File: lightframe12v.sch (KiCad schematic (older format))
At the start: 48 parts, among them J1 PJ-077, J2 Conn_01x06_Female, J3 Conn_01x02_Female, J4 Conn_01x06_Female, J5 Conn_01x04_Female, J6 Conn_01x6_Female, Q1 MMBT2222A-TP, Q2 MMBT2222A-TP, SW1 SW_Push, SW2 SW_Push, U1 ESP32-WROOM-32U, U2 LMR33620Simple, U3 TLC5971

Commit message: Changed schematic to powerbench design
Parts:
- removed C16: 22uF, Capacitor_SMD:C_1206_3216Metric, symbol Device:C_Small
- removed C4: 100uF AL, Capacitor_SMD:CP_Elec_6.3x5.4, symbol Device:CP1_Small
- removed C6: 4.7uF, digikey-footprints:0805, symbol Device:C_Small
- C11: renamed from C13; value 22uF -> 47uF
- C12: renamed from C14; value 22uF -> 47uF
- C14: renamed from C15; value 22uF -> 1uF; footprint Capacitor_SMD:C_1206_3216Metric -> digikey-footprints:0603
- C6: renamed from C8; value 4.7uF -> 10uF
- C7: renamed from C9; value .1uF -> 220nF
- C8: renamed from C10; footprint digikey-footprints:0805 -> digikey-footprints:0603
- L1: value 8.2uH -> 15uH
- R6: value 20k -> 100k
- renumbered C12 to C10, C17 to C13, C18 to C15, C19 to C16, C20 to C17, C21 to C18, C5 to C4, C7 to C5, C11 to C9
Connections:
- wire segments 145 -> 137
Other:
- note added: ".1uF=CC0603KRX7R8BB104 yageo (603)"
- note added: "100kR = RC0603FR-07100KL yageo (603)"
- note added: "10uF=C2012X5R1V106K085AC (805) tdk"
- note added: "1uF = \nC0603C105K8PACTU kemet (603)"
- note added: "1uF=CL10B105KO8NNNC (603)"
- note added: "220nF=C1608X5R1H224K080AB (603) tdk"
- note added: "43.2k=RC0603FR-0743K2L yageo (603)"
- note added: "47uF = GRM31CC80J476KE18L murata (1206)"
- note added: "R6 = RC0603FR-07100KL yageo"
- note added: "inductor =IHLP3232DZER150M11 vishay-dale"
- note removed: ".1uF=CC0603KRX7R8BB104 yageo"
- note removed: "0.1uF=CGA3E2X7R1H104K080AA"
- note removed: "100kR = RC0603FR-07100KL yageo"
- note removed: "1uF = CL21B105KBFNNNG samsung"
- note removed: "20kR = RC0603FR-0720KL yageo"
- note removed: "22uF=CL31A226KAHNNNE samsung"
- note removed: "4.7=C2012X5R1H475K125AB tdk"
- note removed: "43.2k=RC0603FR-0743R2L yageo"
- note removed: "All output caps 25V"
- note removed: "UWT1H101MNL1GS\nfor electrolytic"
- note removed: "all input caps 50V"
- note removed: "inductor =7443330820 wurth"
- moved on the sheet: C11, C12, C14, C8, R6, R7, R8

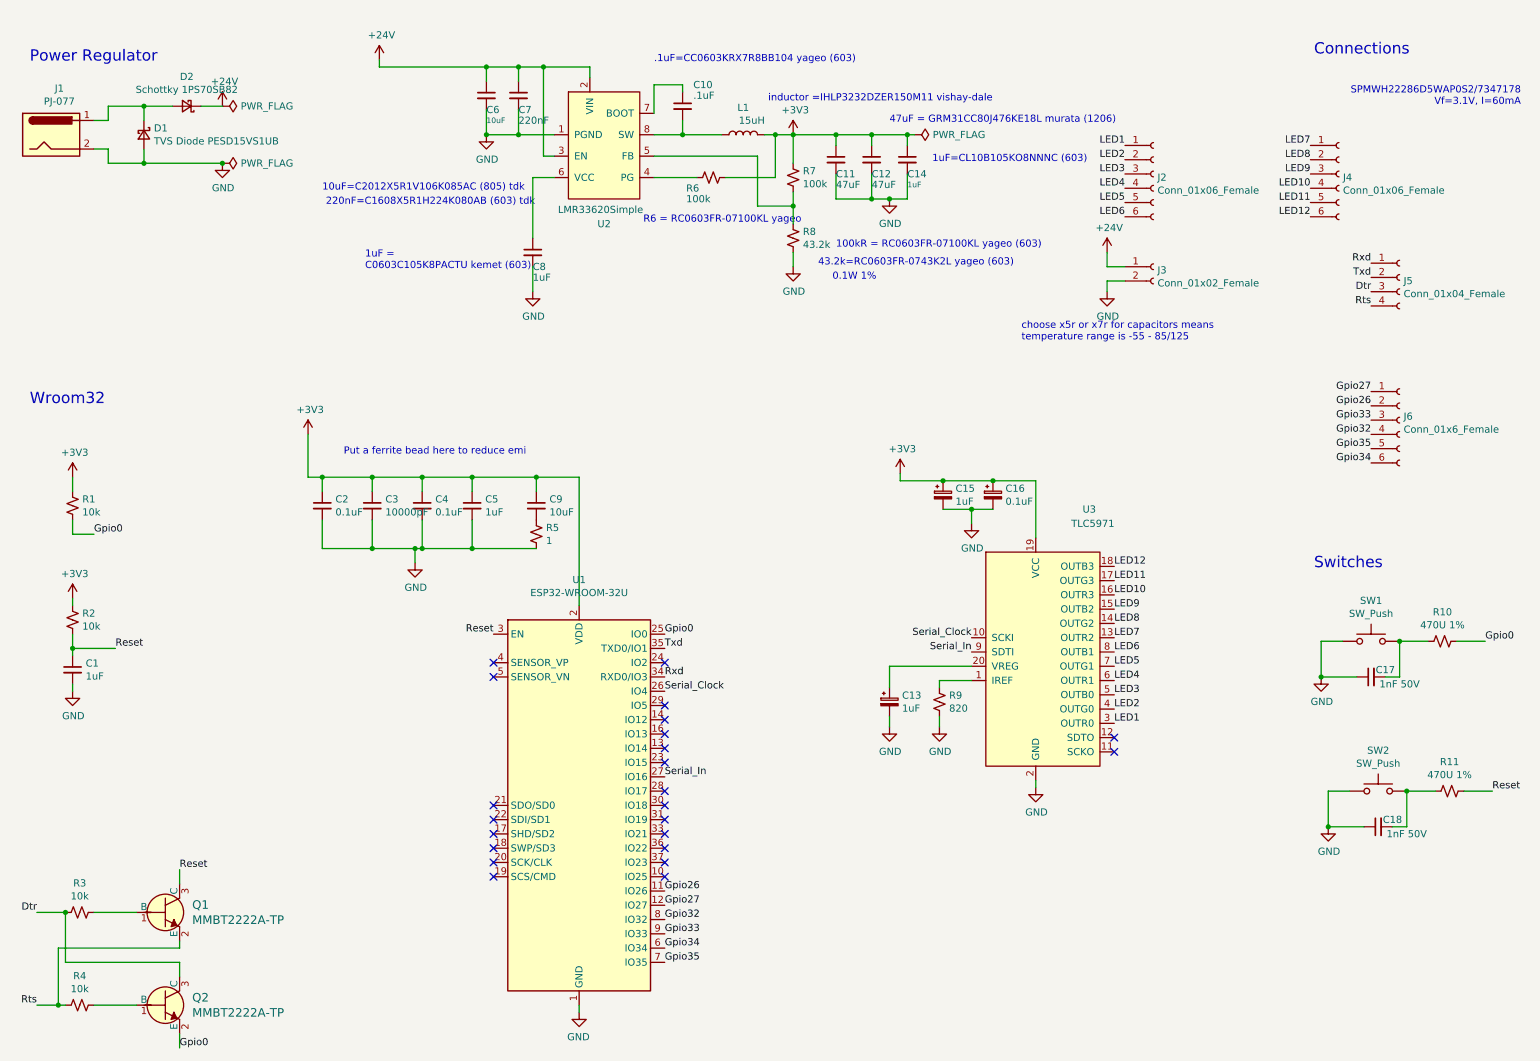
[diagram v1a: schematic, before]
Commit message: Adds new TPS56221 pmic
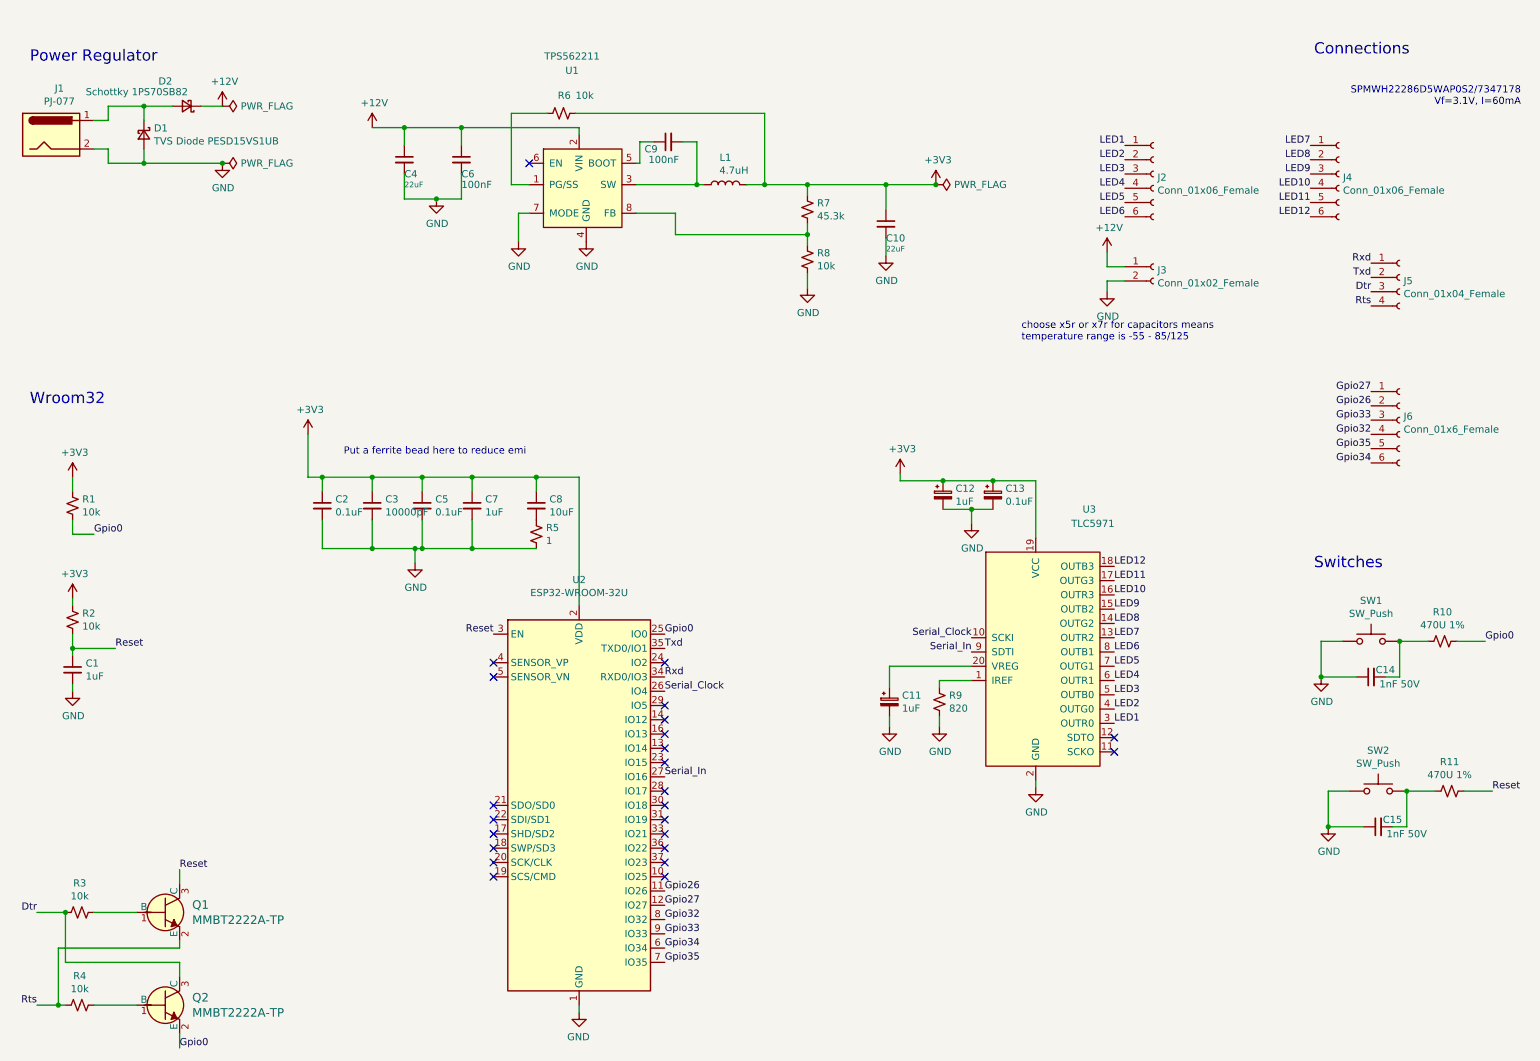
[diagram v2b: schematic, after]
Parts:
- removed C11, C12: 47uF, Capacitor_SMD:C_1206_3216Metric, symbol Device:C_Small
- removed C14, C8: 1uF, digikey-footprints:0603, symbol Device:C_Small
- removed U2: LMR33620Simple, Keith:lmr33620HSOIC, symbol lightframe:LMR33620Simple
- added C9: 100nF, digikey-footprints:0805, symbol Device:C_Small
- added U1: TPS562211, symbol lightframe:TPS562211
- C10: value .1uF -> 22uF; footprint digikey-footprints:0603 -> digikey-footprints:0805
- C4: renamed from C6; value 10uF -> 22uF; footprint digikey-footprints:0805 -> digikey-footprints:1206
- C6: renamed from C7; value 220nF -> 100nF
- L1: value 15uH -> 4.7uH
- R6: value 100k -> 10k
- R7: value 100k -> 45.3k; footprint digikey-footprints:0603 -> Resistor_SMD:R_0402_1005Metric
- R8: value 43.2k -> 10k; footprint digikey-footprints:0603 -> Resistor_SMD:R_0402_1005Metric
- renumbered C13 to C11, C15 to C12, C16 to C13, C17 to C14, C18 to C15, C4 to C5, C5 to C7, C9 to C8, U1 to U2
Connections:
- net +3V3: now also C10.1
- net GND: now also C10.2, U1.4 (GND), U1.7 (MODE)
- net at R6.2: now also U1.1 (PG/SS)
- net at R7.2, R8.1: now also U1.8 (FB)
- net at L1.1: now also C9.2, U1.3 (SW); no longer C10.2
- net +24V renamed +12V
- net +12V: now also U1.2 (VIN)
- new net: C9.1, U1.5 (BOOT)
- no-connect marks 23 -> 24
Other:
- note removed: ".1uF=CC0603KRX7R8BB104 yageo (603)"
- note removed: "0.1W 1%"
- note removed: "100kR = RC0603FR-07100KL yageo (603)"
- note removed: "10uF=C2012X5R1V106K085AC (805) tdk"
- note removed: "1uF = \nC0603C105K8PACTU kemet (603)"
- note removed: "1uF=CL10B105KO8NNNC (603)"
- note removed: "220nF=C1608X5R1H224K080AB (603) tdk"
- note removed: "43.2k=RC0603FR-0743K2L yageo (603)"
- note removed: "47uF = GRM31CC80J476KE18L murata (1206)"
- note removed: "R6 = RC0603FR-07100KL yageo"
- note removed: "inductor =IHLP3232DZER150M11 vishay-dale"
- moved on the sheet: C4, C6, R6, R7

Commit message: Rough layout of pmic
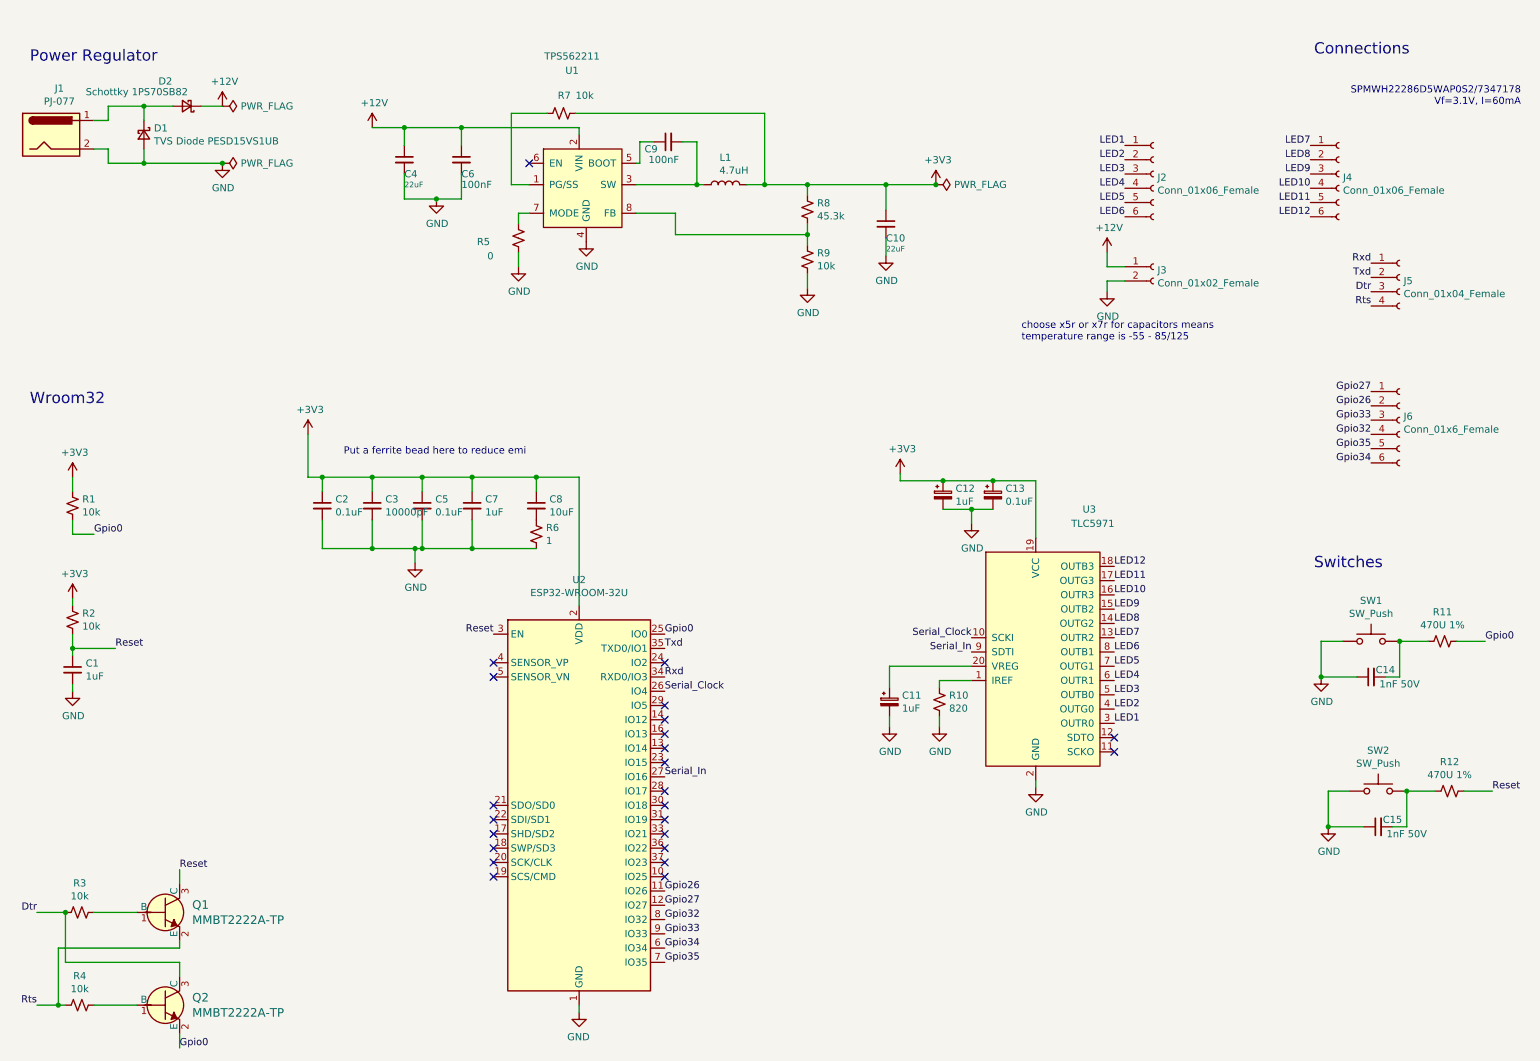
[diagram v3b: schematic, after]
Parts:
- added R5: 0, digikey-footprints:0603, symbol Device:R_Small_US
- L1: footprint Keith:wurth 7443330820 8.2uH -> Keith:SRN8040 Bournes
- U1: footprint (none) -> Keith:TPS562211 12V pmic
- renumbered R9 to R10, R10 to R11, R11 to R12, R5 to R6, R6 to R7, R7 to R8, R8 to R9
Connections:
- net GND: now also R5.1; no longer U1.7 (MODE)
- new net: R5.2, U1.7 (MODE)
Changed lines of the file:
@@
 $EndComp
 $Comp
-L Device:R_Small_US R11
+L Device:R_Small_US R12
 U 1 1 602DA52D
 P 10650 5850
-F 0 "R11" V 10855 5850 50  0000 C CNN
+F 0 "R12" V 10855 5850 50  0000 C CNN
 F 1 "470U 1%" V 10764 5850 50  0000 C CNN
 F 2 "digikey-footprints:0603" H 10650 5850 50  0001 C CNN
@@
 $EndComp
 $Comp
-L Device:R_Small_US R10
+L Device:R_Small_US R11
 U 1 1 6029A6D9
 P 10600 4800
-F 0 "R10" V 10805 4800 50  0000 C CNN
+F 0 "R11" V 10805 4800 50  0000 C CNN
 F 1 "470U 1%" V 10714 4800 50  0000 C CNN
 F 2 "digikey-footprints:0603" H 10600 4800 50  0001 C CNN
@@
 	3100 3950 3100 4150
 $Comp
-L Device:R_Small_US R5
+L Device:R_Small_US R6
 U 1 1 601AF3F3
 P 4250 4050
-F 0 "R5" H 4318 4096 50  0000 L CNN
+F 0 "R6" H 4318 4096 50  0000 L CNN
 F 1 "1" H 4318 4005 50  0000 L CNN
 F 2 "Resistor_SMD:R_0402_1005Metric" H 4250 4050 50  0001 C CNN
@@
 LED12
 $Comp
-L Device:R_Small_US R9
+L Device:R_Small_US R10
 U 1 1 60526411
 P 7075 5225
-F 0 "R9" H 7143 5271 50  0000 L CNN
+F 0 "R10" H 7143 5271 50  0000 L CNN
 F 1 "820" H 7143 5180 50  0000 L CNN
 F 2 "digikey-footprints:0603" H 7075 5225 50  0001 C CNN
@@
 $EndComp
 $Comp
-L Device:R_Small_US R7
+L Device:R_Small_US R8
 U 1 1 605822D2
 P 6150 1775
-F 0 "R7" H 6218 1821 50  0000 L CNN
+F 0 "R8" H 6218 1821 50  0000 L CNN
 F 1 "45.3k" H 6218 1730 50  0000 L CNN
 F 2 "Resistor_SMD:R_0402_1005Metric" H 6150 1775 50  0001 C CNN
@@
 F 0 "L1" V 5765 1600 50  0000 C CNN
 F 1 "4.7uH" V 5675 1540 50  0000 C CNN
-F 2 "Keith:wurth 7443330820 8.2uH" H 5575 1600 50  0001 C CNN
+F 2 "Keith:SRN8040 Bournes" H 5575 1600 50  0001 C CNN
 F 3 "~" H 5575 1600 50  0001 C CNN
 	1    5575 1600
@@
 $EndComp
 $Comp
-L Device:R_Small_US R8
+L Device:R_Small_US R9
 U 1 1 6058B282
 P 6150 2125
-F 0 "R8" H 6218 2171 50  0000 L CNN
+F 0 "R9" H 6218 2171 50  0000 L CNN
 F 1 "10k" H 6218 2080 50  0000 L CNN
 F 2 "Resistor_SMD:R_0402_1005Metric" H 6150 2125 50  0001 C CNN
@@
 L power:GND #PWR010
 U 1 1 6067EF84
-P 4125 2000
-F 0 "#PWR010" H 4125 1750 50  0001 C CNN
-F 1 "GND" H 4130 1827 50  0000 C CNN
-F 2 "" H 4125 2000 50  0001 C CNN
-F 3 "" H 4125 2000 50  0001 C CNN
-	1    4125 2000
+P 4125 2175
+F 0 "#PWR010" H 4125 1925 50  0001 C CNN
+F 1 "GND" H 4130 2002 50  0000 C CNN
+F 2 "" H 4125 2175 50  0001 C CNN
+F 3 "" H 4125 2175 50  0001 C CNN
+	1    4125 2175
 	1    0    0    -1
 $EndComp
@@
 	4200 1800 4125 1800
 Wire Wire Line
-	4125 1800 4125 2000
+	4125 1800 4125 1875
 Wire Wire Line
 	6150 1600 6700 1600
@@
 	4075 1100 4325 1100
 $Comp
-L Device:R_Small_US R6
+L Device:R_Small_US R7
 U 1 1 60575D24
 P 4425 1100
-F 0 "R6" V 4300 1075 50  0000 L CNN
+F 0 "R7" V 4300 1075 50  0000 L CNN
 F 1 "10k" V 4300 1200 50  0000 L CNN
 F 2 "digikey-footprints:0603" H 4425 1100 50  0001 C CNN
@@
 $EndComp
 NoConn ~ 4200 1450
+Connection ~ 7050 1600
+$Comp
+L Device:R_Small_US R5
+U 1 1 60589E1C
+P 4125 1975
+F 0 "R5" H 4325 2000 50  0000 L CNN
+F 1 "0" H 4300 2100 50  0000 L CNN
+F 2 "digikey-footprints:0603" H 4125 1975 50  0001 C CNN
+F 3 "~" H 4125 1975 50  0001 C CNN
+	1    4125 1975
+	-1   0    0    1
+$EndComp
+Wire Wire Line
+	4125 2075 4125 2175
 $Comp
 L lightframe:TPS562211 U1
@@
 F 0 "U1" H 4500 2400 50  0000 C CNN
 F 1 "TPS562211" H 4500 2500 50  0000 C CNN
-F 2 "" H 4550 1600 50  0001 C CNN
+F 2 "Keith:TPS562211 12V pmic" H 4550 1600 50  0001 C CNN
 F 3 "" H 4550 1600 50  0001 C CNN
 	1    4550 1600
 	1    0    0    -1
 $EndComp
-Connection ~ 7050 1600
 $EndSCHEMATC
